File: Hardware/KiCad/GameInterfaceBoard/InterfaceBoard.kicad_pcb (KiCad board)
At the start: 2 copper layers, 152.4 x 110.5 mm, 37 parts, among them J1 CONN_11LOCK, J2 CONN_07LOCK

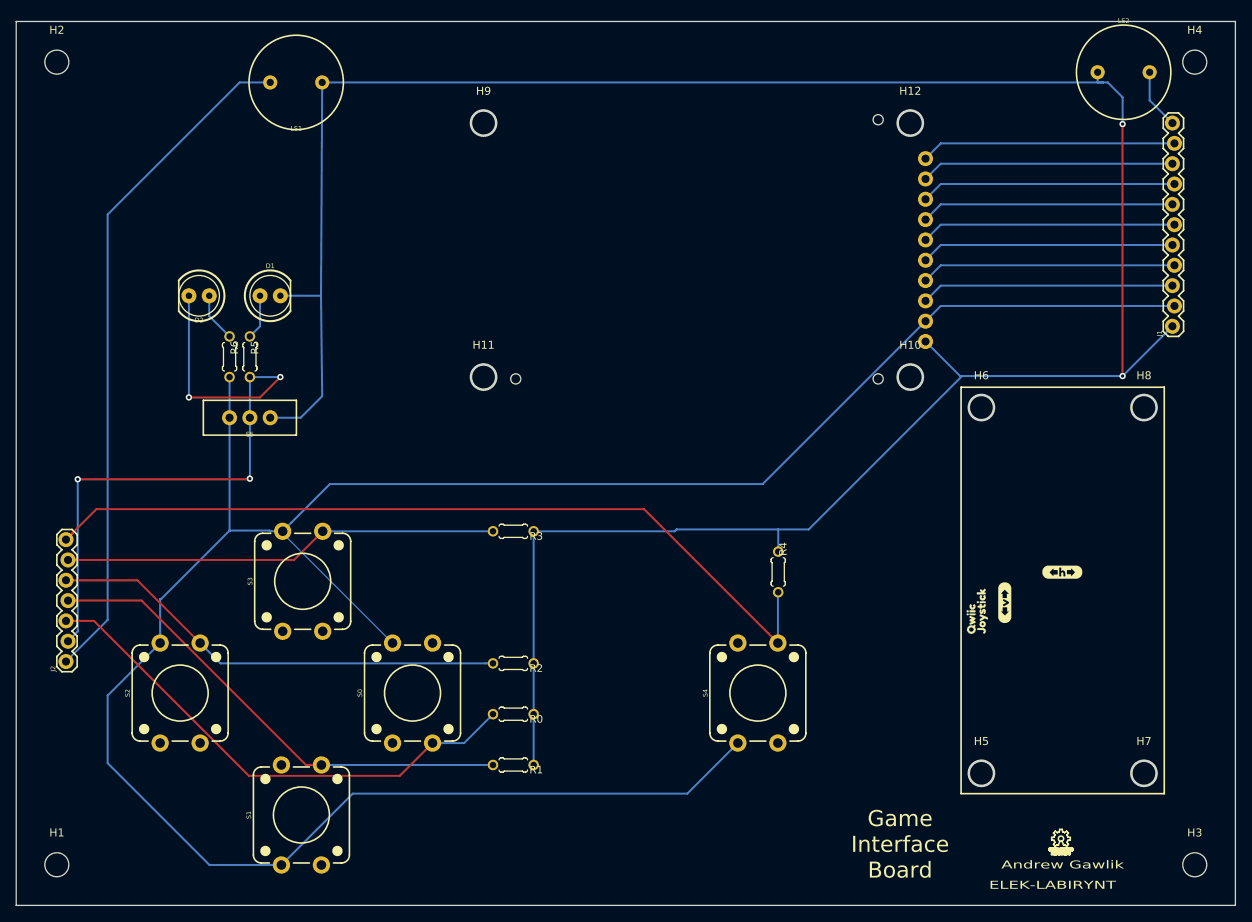
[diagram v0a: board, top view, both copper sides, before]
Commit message: Removed excess drill holes as requested on issue #17
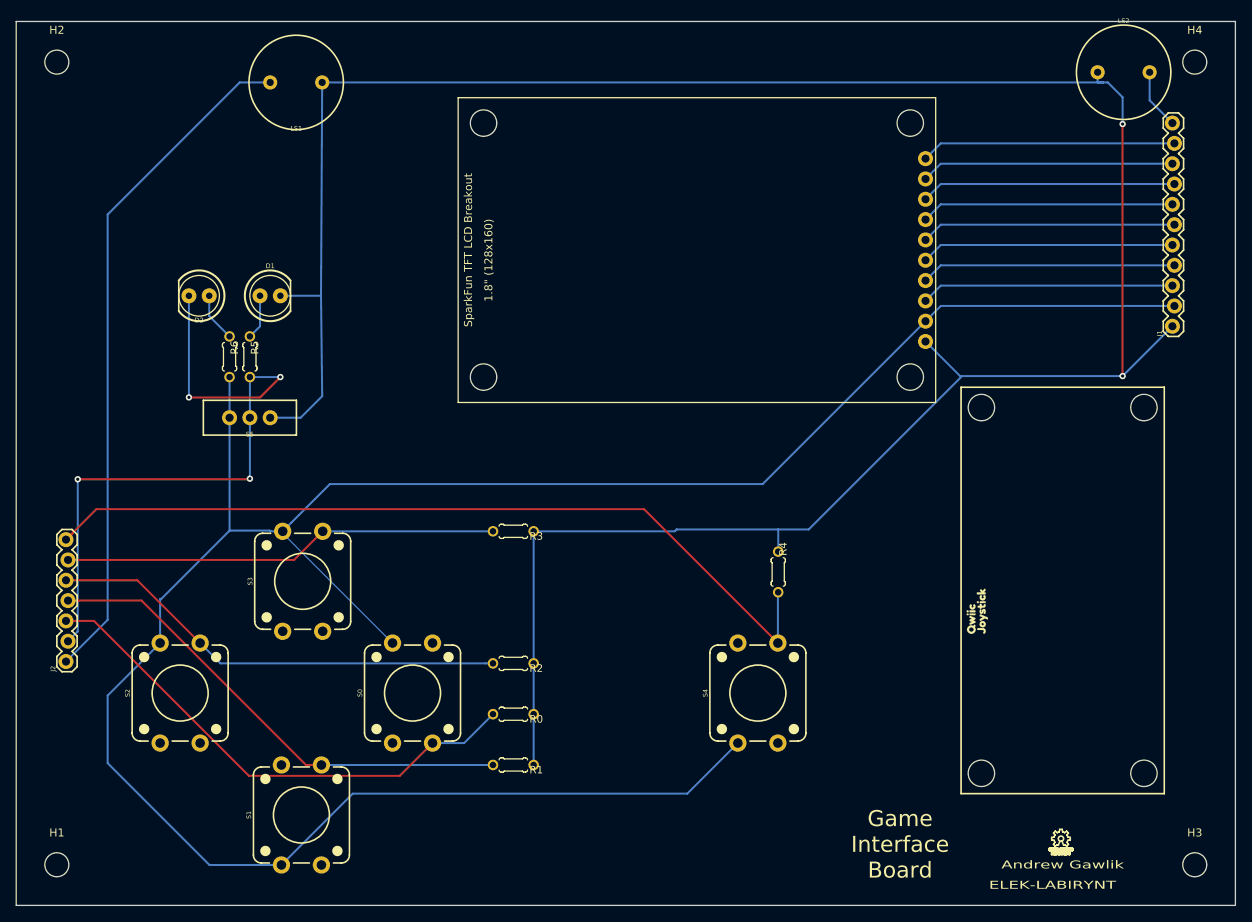
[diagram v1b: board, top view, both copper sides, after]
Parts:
- removed H10, H11, H12, H5, H6, H7, H8, H9: MountingHole, MountingHole:MountingHole_3mm
